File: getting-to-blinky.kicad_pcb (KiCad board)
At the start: 2 copper layers, 30 x 22.8 mm, 11 parts, among them SW1 JS202011SCQN, U1 ICM7555

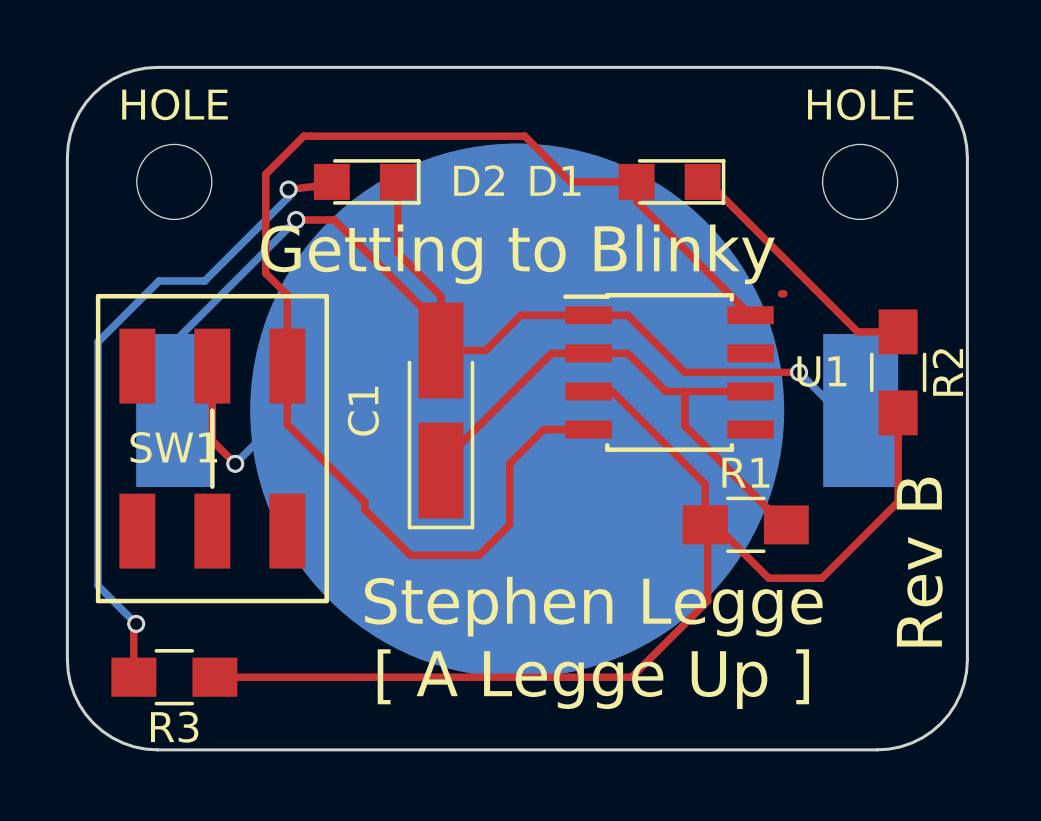
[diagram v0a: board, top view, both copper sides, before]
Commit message: Update with corrected battery polarity and added GND and VCC planes
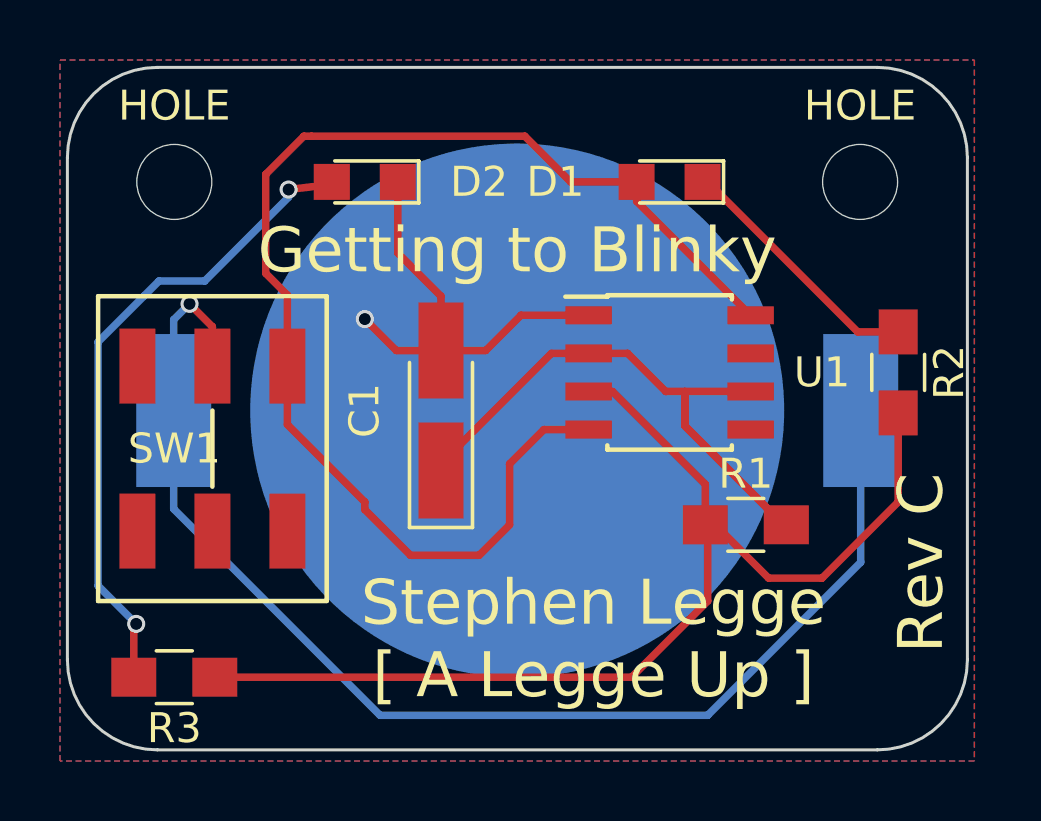
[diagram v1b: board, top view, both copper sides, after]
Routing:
- net Net-(BT1-Pad1): track 13.9 -> 45.6 mm
- net GND: track 37.1 -> 29.4 mm, vias 2 -> 1
- added copper zone on B.Cu, net GND
- added copper zone on F.Cu, net VCC
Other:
- board text added: "Rev C"
- board text removed: "Rev B"
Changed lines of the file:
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@@
     (thickness 1.6)
     (drawings 11)
-    (tracks 88)
+    (tracks 89)
     (zones 0)
     (modules 11)
@@
     (add_net VCC)
   )
-  (module ALU_Connectors:BAT-HLD-001-CR2032 (layer B.Cu)
-    (at 148.59 100.33)
-    (fp_text reference BT1 (at -7.62 -9.144) (layer B.SilkS)
-      (effects (font (size 1 1) (thickness 0.15)) (justify mirror))
-    )
-    (fp_text value Battery_Cell (at 0 11.43) (layer B.Fab)
-      (effects (font (size 1 1) (thickness 0.15)) (justify mirror))
-    )
-    (fp_line (start -13.97 10.16) (end 13.97 10.16) (layer B.SilkS) (width 0.15))
-    (fp_line (start 13.97 10.16) (end 13.97 -10.16) (layer B.SilkS) (width 0.15))
-    (fp_line (start 13.97 -10.16) (end -13.97 -10.16) (layer B.SilkS) (width 0.15))
-    (fp_line (start -13.97 -10.16) (end -13.97 10.16) (layer B.SilkS) (width 0.15))
-    (pad 2 smd rect (at 11.45 0) (size 2.5 5.1) (layers B.Cu B.Paste B.Mask)
-      (net 1 GND))
-    (pad 2 smd rect (at -11.45 0) (size 2.5 5.1) (layers B.Cu B.Paste B.Mask)
-      (net 1 GND))
-    (pad 1 smd circle (at 0 0) (size 17.8 17.8) (layers B.Cu B.Paste B.Mask)
-      (net 7 "Net-(BT1-Pad1)"))
-  )
   (module Capacitors_Tantalum_SMD:CP_Tantalum_Case-A_EIA-3216-18_Hand (layer F.Cu)
     (at 146.05 100.33 90)
@@
     (pad 6 smd rect (at 2.5 -2.75 180) (size 1.2 2.5) (layers F.Cu F.Paste F.Mask))
   )
+  (module ALU_Connectors:BAT-HLD-001-CR2032 (layer B.Cu)
+    (at 148.59 100.33)
+    (fp_text reference BT1 (at -11.43 -8.89) (layer B.SilkS)
+      (effects (font (size 1 1) (thickness 0.15)) (justify mirror))
+    )
+    (fp_text value Battery_Cell (at 0 11.43) (layer B.Fab)
+      (effects (font (size 1 1) (thickness 0.15)) (justify mirror))
+    )
+    (fp_line (start -13.97 10.16) (end 13.97 10.16) (layer B.SilkS) (width 0.15))
+    (fp_line (start 13.97 10.16) (end 13.97 -10.16) (layer B.SilkS) (width 0.15))
+    (fp_line (start 13.97 -10.16) (end -13.97 -10.16) (layer B.SilkS) (width 0.15))
+    (fp_line (start -13.97 -10.16) (end -13.97 10.16) (layer B.SilkS) (width 0.15))
+    (pad 1 smd rect (at 11.45 0) (size 2.5 5.1) (layers B.Cu B.Paste B.Mask)
+      (net 7 "Net-(BT1-Pad1)"))
+    (pad 1 smd rect (at -11.45 0) (size 2.5 5.1) (layers B.Cu B.Paste B.Mask)
+      (net 7 "Net-(BT1-Pad1)"))
+    (pad 2 smd circle (at 0 0) (size 17.8 17.8) (layers B.Cu B.Paste B.Mask)
+      (net 1 GND))
+  )
   (gr_arc (start 160.5964 91.892) (end 163.5964 91.892) (angle -90) (layer Edge.Cuts) (width 0.1))
   (gr_line (start 163.5964 108.642) (end 163.5964 91.892) (layer Edge.Cuts) (width 0.1))
@@
   (gr_arc (start 136.5964 91.892) (end 136.5964 88.892) (angle -90) (layer Edge.Cuts) (width 0.1))
   (gr_line (start 160.5964 88.892) (end 136.5964 88.892) (layer Edge.Cuts) (width 0.1))
-  (gr_text "Rev B" (at 162.052 105.41 90) (layer F.SilkS)
+  (gr_text "Rev C" (at 162.052 105.41 90) (layer F.SilkS)
     (effects (font (size 1.5 1.5) (thickness 0.3)))
   )
@@
     (effects (font (size 1.5 1.5) (thickness 0.3)))
   )
-  (segment (start 157.48 96.44) (end 157.4 96.44) (width 0.25) (layer F.Cu) (net 0))
   (segment (start 135.93 98.85) (end 135.934 98.85) (width 0.25) (layer F.Cu) (net 0))
+  (segment (start 146.05 98.33) (end 144.558 98.33) (width 0.25) (layer F.Cu) (net 1) (status 400000))
+  (segment (start 143.51 97.282) (end 146.558 100.33) (width 0.25) (layer B.Cu) (net 1) (status 800000))
+  (via (at 143.51 97.282) (size 0.6) (drill 0.4) (layers F.Cu B.Cu) (net 1))
+  (segment (start 144.558 98.33) (end 143.51 97.282) (width 0.25) (layer F.Cu) (net 1))
+  (segment (start 146.558 100.33) (end 148.59 100.33) (width 0.25) (layer B.Cu) (net 1) (status C00000))
   (segment (start 146.05 98.33) (end 146.05 97.536) (width 0.25) (layer F.Cu) (net 1))
-  (segment (start 146.05 97.536) (end 142.494 93.98) (width 0.25) (layer F.Cu) (net 1))
-  (segment (start 141.224 93.98) (end 137.14 98.064) (width 0.25) (layer B.Cu) (net 1))
-  (via (at 141.224 93.98) (size 0.6) (drill 0.4) (layers F.Cu B.Cu) (net 1))
-  (segment (start 142.494 93.98) (end 141.224 93.98) (width 0.25) (layer F.Cu) (net 1))
-  (segment (start 137.14 98.064) (end 137.14 100.33) (width 0.25) (layer B.Cu) (net 1))
-  (segment (start 150.97 97.155) (end 152.273 97.155) (width 0.25) (layer F.Cu) (net 1))
-  (segment (start 157.988 99.06) (end 159.258 100.33) (width 0.25) (layer B.Cu) (net 1) (status 20))
-  (via (at 157.988 99.06) (size 0.6) (drill 0.4) (layers F.Cu B.Cu) (net 1))
-  (segment (start 154.178 99.06) (end 157.988 99.06) (width 0.25) (layer F.Cu) (net 1))
-  (segment (start 152.273 97.155) (end 154.178 99.06) (width 0.25) (layer F.Cu) (net 1))
-  (segment (start 159.258 100.33) (end 160.04 100.33) (width 0.25) (layer B.Cu) (net 1) (status 30))
   (segment (start 146.05 98.33) (end 147.542 98.33) (width 0.25) (layer F.Cu) (net 1))
   (segment (start 148.717 97.155) (end 150.97 97.155) (width 0.25) (layer F.Cu) (net 1))
@@
   (segment (start 144.61 95.08) (end 144.61 92.71) (width 0.25) (layer F.Cu) (net 1))
   (segment (start 146.05 96.52) (end 144.61 95.08) (width 0.25) (layer F.Cu) (net 1))
+  (segment (start 140.97 100.33) (end 148.59 100.33) (width 0.25) (layer B.Cu) (net 1))
   (segment (start 141.732 91.186) (end 141.478 91.186) (width 0.25) (layer F.Cu) (net 2))
   (segment (start 148.844 91.186) (end 141.732 91.186) (width 0.25) (layer F.Cu) (net 2))
@@
   (segment (start 149.86 109.22) (end 152.4 109.22) (width 0.25) (layer F.Cu) (net 6))
   (segment (start 154.94 104.22) (end 154.86 104.14) (width 0.25) (layer F.Cu) (net 6))
-  (segment (start 138.43 98.85) (end 138.43 101.346) (width 0.25) (layer F.Cu) (net 7))
-  (segment (start 139.192 102.108) (end 140.97 100.33) (width 0.25) (layer B.Cu) (net 7))
-  (via (at 139.192 102.108) (size 0.6) (drill 0.4) (layers F.Cu B.Cu) (net 7))
-  (segment (start 138.43 101.346) (end 139.192 102.108) (width 0.25) (layer F.Cu) (net 7))
-  (segment (start 140.97 100.33) (end 148.59 100.33) (width 0.25) (layer B.Cu) (net 7))
+  (segment (start 160.04 105.39) (end 160.04 100.33) (width 0.25) (layer B.Cu) (net 7))
+  (segment (start 154.94 110.49) (end 160.04 105.39) (width 0.25) (layer B.Cu) (net 7))
+  (segment (start 144.018 110.49) (end 154.94 110.49) (width 0.25) (layer B.Cu) (net 7))
+  (segment (start 137.14 103.612) (end 144.018 110.49) (width 0.25) (layer B.Cu) (net 7))
+  (segment (start 137.14 100.33) (end 137.14 103.612) (width 0.25) (layer B.Cu) (net 7))
+  (segment (start 138.43 97.536) (end 138.43 98.85) (width 0.25) (layer F.Cu) (net 7))
+  (segment (start 137.668 96.774) (end 138.43 97.536) (width 0.25) (layer F.Cu) (net 7))
+  (via (at 137.668 96.774) (size 0.6) (drill 0.4) (layers F.Cu B.Cu) (net 7))
+  (segment (start 137.14 97.302) (end 137.668 96.774) (width 0.25) (layer B.Cu) (net 7))
+  (segment (start 137.14 100.33) (end 137.14 97.302) (width 0.25) (layer B.Cu) (net 7))
+  (segment (start 137.14 98.064) (end 137.14 100.33) (width 0.25) (layer B.Cu) (net 7))
+  (segment (start 159.258 100.33) (end 160.04 100.33) (width 0.25) (layer B.Cu) (net 7) (status 30))
   (segment (start 138.43 98.85) (end 138.43 99.06) (width 0.25) (layer F.Cu) (net 7))
+  (zone (net 1) (net_name GND) (layer B.Cu) (hatch edge 0.508)
+    (connect_pads (clearance 0.508))
+    (min_thickness 0.254)
+    (fill yes (arc_segments 16) (thermal_gap 0.508) (thermal_bridge_width 0.508))
+    (polygon
+      (pts
+        (xy 163.83 112.014) (xy 133.35 112.014) (xy 133.35 88.646) (xy 163.83 88.646)
+      )
+    )
+  )
+  (zone (net 2) (net_name VCC) (layer F.Cu) (hatch edge 0.508)
+    (connect_pads (clearance 0.508))
+    (min_thickness 0.254)
+    (fill yes (arc_segments 16) (thermal_gap 0.508) (thermal_bridge_width 0.508))
+    (polygon
+      (pts
+        (xy 163.83 112.014) (xy 133.35 112.014) (xy 133.35 88.646) (xy 163.83 88.646)
+      )
+    )
+  )
 )

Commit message: Finalized and cleaned up the schematic and layed out Rev C
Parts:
- removed the HOLE at (160.0, 92.7)
- added Q1: BC808-40, TO_SOT_Packages_SMD:SOT-23, F.Cu at (179.1, 130.8)
- added Q2: BC818-40, TO_SOT_Packages_SMD:SOT-23, F.Cu at (198.1, 128.3)
- added R4: 470, Resistors_SMD:R_0805_HandSoldering, F.Cu at (195.6, 132.1)
- added R5: 1.2K, Resistors_SMD:R_0805_HandSoldering, F.Cu at (182.9, 139.7)
- added R6: 720, Resistors_SMD:R_0805_HandSoldering, F.Cu at (174.0, 132.1)
- added R7: 1.2K, Resistors_SMD:R_0805_HandSoldering, F.Cu at (186.7, 139.7)
- added R8: 720, Resistors_SMD:R_0805_HandSoldering, F.Cu at (185.2, 128.5)
- R1: value R -> 110K
- R2, R3: value R -> 55
- moved SW1 68.5 mm to (193.6, 142.2)
- moved HOLE 57.0 mm to (186.8, 120.7)
- moved BT1 51.3 mm to (187.2, 134.1)
- moved C1 50.4 mm to (178.8, 138.6)
- moved R1 49.8 mm to (195.6, 134.6), turned to 180 degrees
- moved D1 49.0 mm to (193.0, 121.9)
- moved U1 48.0 mm to (187.5, 133.1)
- moved D2 47.0 mm to (180.3, 121.9)
- moved R3 47.0 mm to (174.0, 138.4), turned to 270 degrees
- moved R2 42.2 mm to (191.5, 128.5), turned to 0 degrees
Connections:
- D1 pad 2: VCC -> Net-(D1-Pad2)
- R2 pad 1: Net-(D1-Pad1) -> Net-(D1-Pad2)
- R2 pad 2: Net-(R1-Pad1) -> VCC
- R3 pad 1: Net-(R1-Pad1) -> Net-(D2-Pad2)
- R3 pad 2: Net-(D2-Pad2) -> Net-(Q1-Pad2)
- U1 pad 3: Net-(R1-Pad1) -> /OUT
- U1 pad 7: (no net) -> Net-(R1-Pad1)
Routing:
- net Net-(Q2-Pad1): track 0.00 -> 62.8 mm, vias 0 -> 4
- net Net-(Q1-Pad1): track 0.00 -> 31.7 mm, vias 0 -> 2
- net Net-(R1-Pad1): track 37.8 -> 9.76 mm
- net Net-(BT1-Pad1): track 45.6 -> 18.8 mm
- net VCC: track 43.1 -> 56.1 mm
- net /OUT: track 0.00 -> 11.6 mm
- net Net-(Q1-Pad2): track 0.00 -> 9.71 mm
- net Net-(D1-Pad2): track 0.00 -> 7.34 mm
- net GND: track 29.4 -> 35.1 mm, vias 1 -> 3
- net Drain: track 25.0 -> 21.5 mm
- net Net-(D2-Pad2): track 21.9 -> 19.3 mm, vias 2 -> 0
- net Net-(D1-Pad1): track 8.59 -> 9.56 mm
- added copper zone on F.Cu, net GND
- added copper zone on B.Cu, net Net-(BT1-Pad1)
- removed copper zone on B.Cu, net GND
- removed copper zone on F.Cu, net VCC
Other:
- board size 30 x 22.8 mm -> 33.7 x 33.7 mm

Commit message: Luckily caught the pads mask clearance before ordering
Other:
- rule pad_to_mask_clearance: 0.2 -> 0
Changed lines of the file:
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@@
     (links 28)
     (no_connects 0)
-    (area 170.010975 117.686975 203.877025 151.553025)
+    (area 160.99 111.41 210.790001 153.610001)
     (thickness 1.6)
     (drawings 4)
@@
     (pad_size 1.524 1.524)
     (pad_drill 0.762)
-    (pad_to_mask_clearance 0.2)
+    (pad_to_mask_clearance 0)
     (aux_axis_origin 128.27 81.534)
     (grid_origin 148.59 105.41)
@@
     (effects (font (size 1.5 1.5) (thickness 0.3)))
   )
-  (segment (start 186.516 128.524) (end 186.516 127.484) (width 0.25) (layer F.Cu) (net 1) (status 400000))
-  (segment (start 187.59 126.41) (end 187.198 126.802) (width 0.25) (layer B.Cu) (net 1) (status 800000))
+  (segment (start 186.516 128.524) (end 186.516 127.484) (width 0.25) (layer F.Cu) (net 1))
+  (segment (start 187.59 126.41) (end 187.198 126.802) (width 0.25) (layer B.Cu) (net 1))
   (via (at 187.59 126.41) (size 0.6) (drill 0.4) (layers F.Cu B.Cu) (net 1))
   (segment (start 186.516 127.484) (end 187.59 126.41) (width 0.25) (layer F.Cu) (net 1))
-  (segment (start 187.198 126.802) (end 187.198 134.112) (width 0.25) (layer B.Cu) (net 1) (status C00000))
+  (segment (start 187.198 126.802) (end 187.198 134.112) (width 0.25) (layer B.Cu) (net 1))
   (segment (start 184.752 131.191) (end 182.809 131.191) (width 0.25) (layer F.Cu) (net 1))
   (segment (start 181.59 132.41) (end 183.292 134.112) (width 0.25) (layer B.Cu) (net 1))
@@
   (segment (start 173.99 139.68) (end 173.99 139.78) (width 0.25) (layer F.Cu) (net 10))
   (segment (start 175.139991 135.340009) (end 175.139991 138.530009) (width 0.25) (layer F.Cu) (net 10))
-  (segment (start 183.816 128.524) (end 183.816 128.036) (width 0.25) (layer F.Cu) (net 11) (status C00000))
-  (segment (start 183.816 128.036) (end 182.59 126.81) (width 0.25) (layer F.Cu) (net 11) (status 400000))
-  (segment (start 186.69 142.11) (end 186.69 141.05) (width 0.25) (layer F.Cu) (net 11) (status 800000))
+  (segment (start 183.816 128.524) (end 183.816 128.036) (width 0.25) (layer F.Cu) (net 11))
+  (segment (start 183.816 128.036) (end 182.59 126.81) (width 0.25) (layer F.Cu) (net 11))
+  (segment (start 186.69 142.11) (end 186.69 141.05) (width 0.25) (layer F.Cu) (net 11))
   (segment (start 188.99 144.41) (end 186.69 142.11) (width 0.25) (layer F.Cu) (net 11))
   (via (at 188.99 144.41) (size 0.6) (drill 0.4) (layers F.Cu B.Cu) (net 11))
